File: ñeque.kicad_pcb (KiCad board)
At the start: 2 copper layers, 45.5 x 41.3 mm, 8 parts, among them IC1 MIC1555YM5-TR

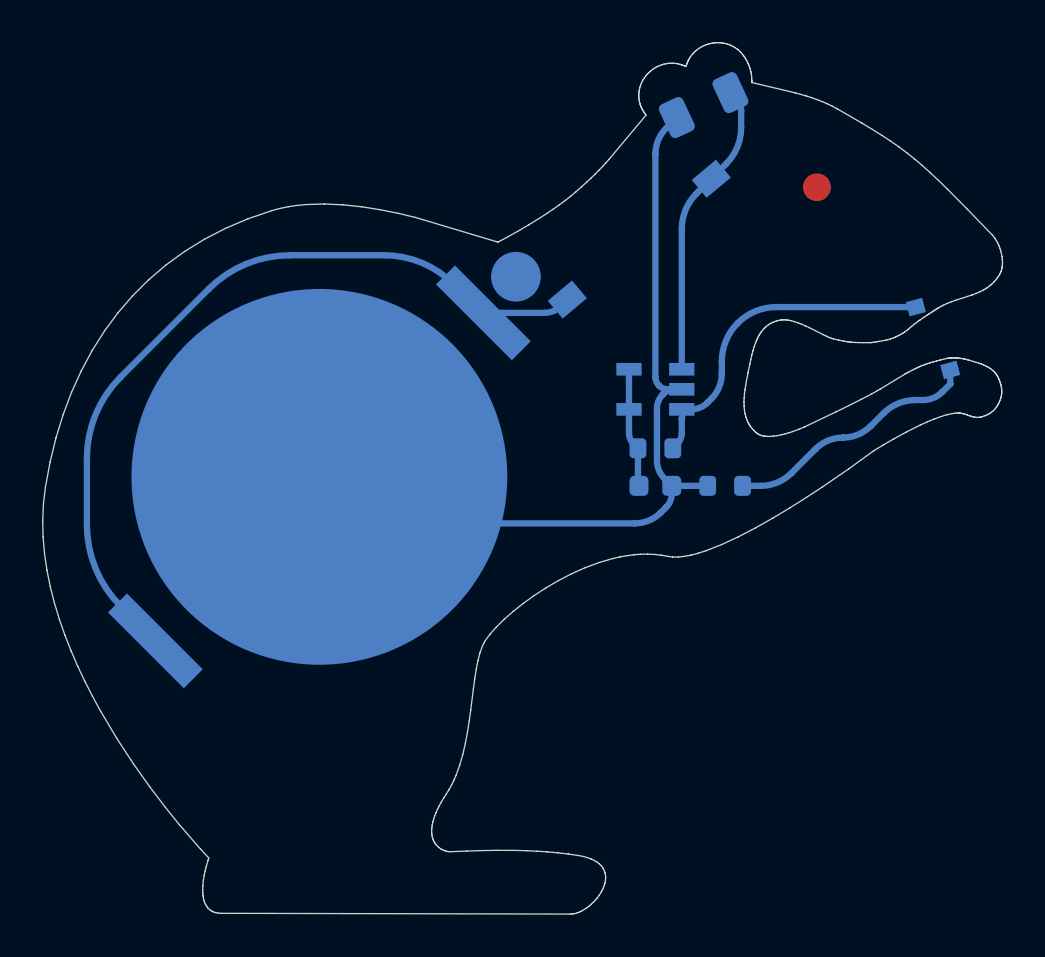
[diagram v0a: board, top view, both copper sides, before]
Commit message: fixed resistor + LED
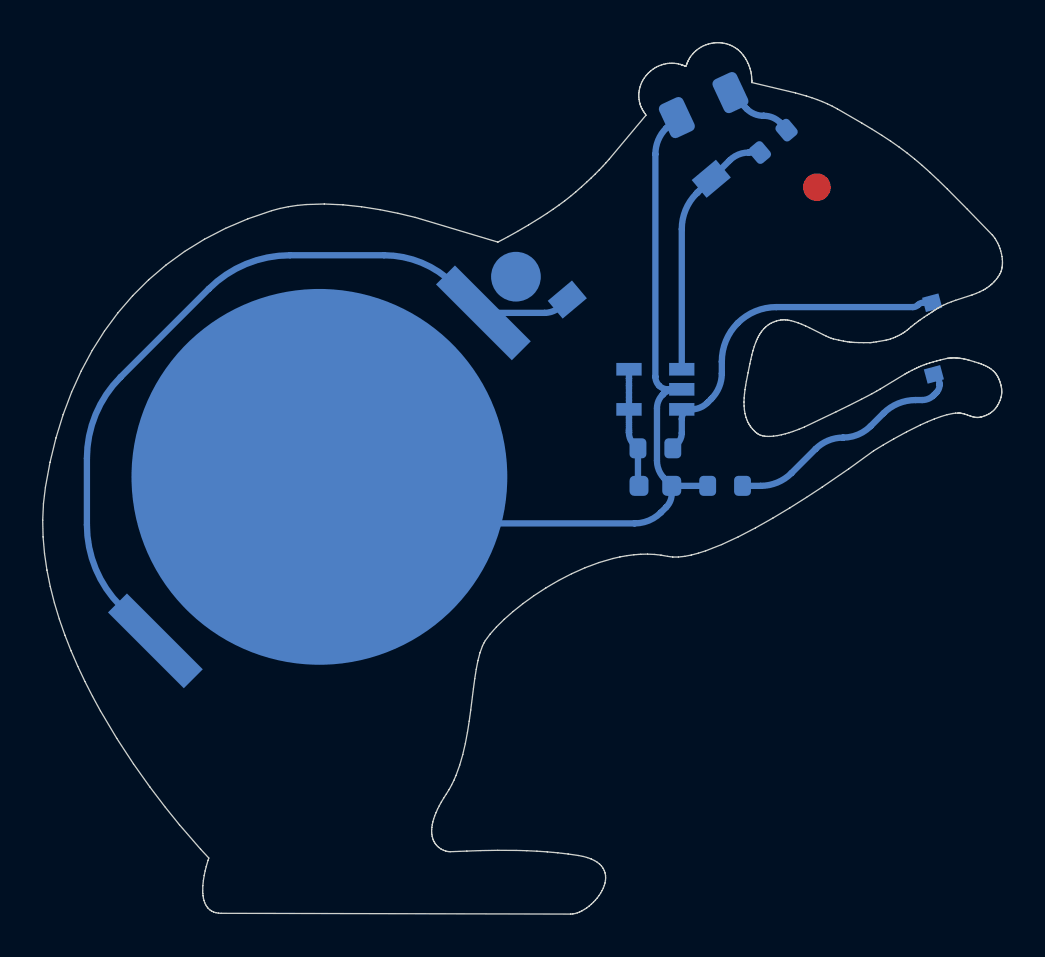
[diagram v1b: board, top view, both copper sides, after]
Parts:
- added R3: 220, Resistor_SMD:R_0603_1608Metric, B.Cu at (169.4, 90.1)
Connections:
- D1 pad 2: +3V0 -> Net-(D1-Pad2)
- S1 pad 2: Net-(S1-Pad2) -> Net-(BT1-Pad1)
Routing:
- net Net-(D1-Pad2): track 0.00 -> 3.32 mm
- net +3V0: track 13.5 -> 11.5 mm
- net Net-(D2-Pad2): track 15.9 -> 16.7 mm
